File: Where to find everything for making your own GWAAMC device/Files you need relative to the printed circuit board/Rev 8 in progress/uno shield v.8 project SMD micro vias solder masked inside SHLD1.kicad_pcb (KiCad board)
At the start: 2 copper layers, 68.6 x 53.3 mm, 82 parts, among them J1 Conn_3.5mm, J2 Power, J3 Analog, J4 Digital, J5 Digital, J6 Conn_01x09_Female, J6_A7,A6 Conn_01x02_gender_unknown, J7_A7,A6 Conn_01x02_Female, J9 TE_1-2328702-0, P1 CONN_01X01, P2 CONN_01X01, P3 CONN_01X01, P4 CONN_01X01, Q1 MMBF5460 (2N5460), Q2 MMBF5460 (2N5460), Q3 DMN601K-7, Q4 DMN601K-7, Q5 DMN601K-7, Q6 DMN601K-7, Q7 DMN601K-7, U1 3V LDO, U2 AD8244ARMZ, U3 ADL5315ACPZ-R7, U4 REF200AU, U5 LM334M, U6 LM334M, U7 MCP4262-503E/UN, U8 - U32 all in parallel MCP4262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

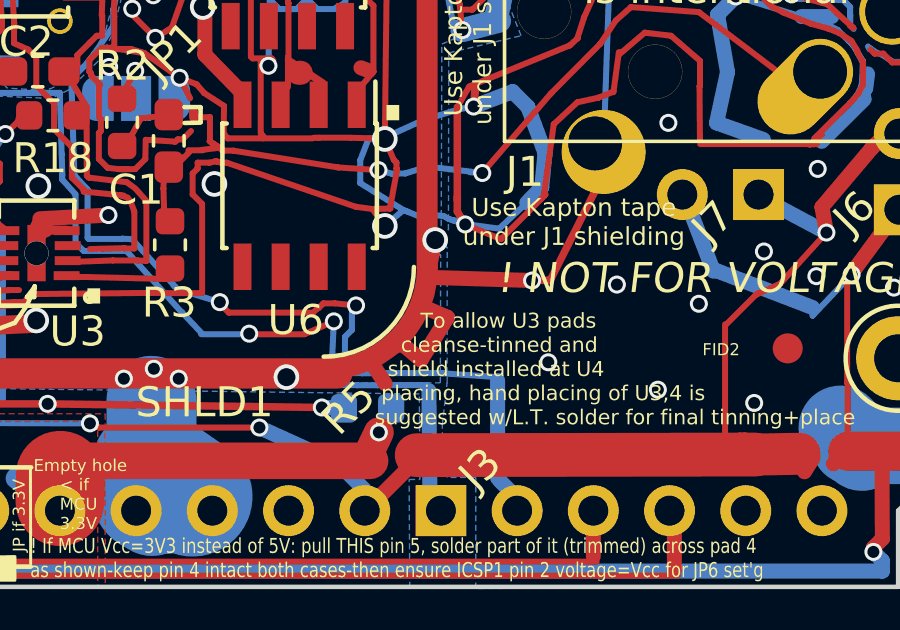
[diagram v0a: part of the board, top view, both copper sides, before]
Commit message: Untested while awaiting bare PCB boards....
These KiCad and zipped gerber files are fully designed but not yet tested while I await the bare boards on order now.  I'm estimating mid- to late-October will see the final evaluation of operation of the entire device.  Shortly after that, I would expect to demonstrate its concepts and operation via YouTube and personal travel.
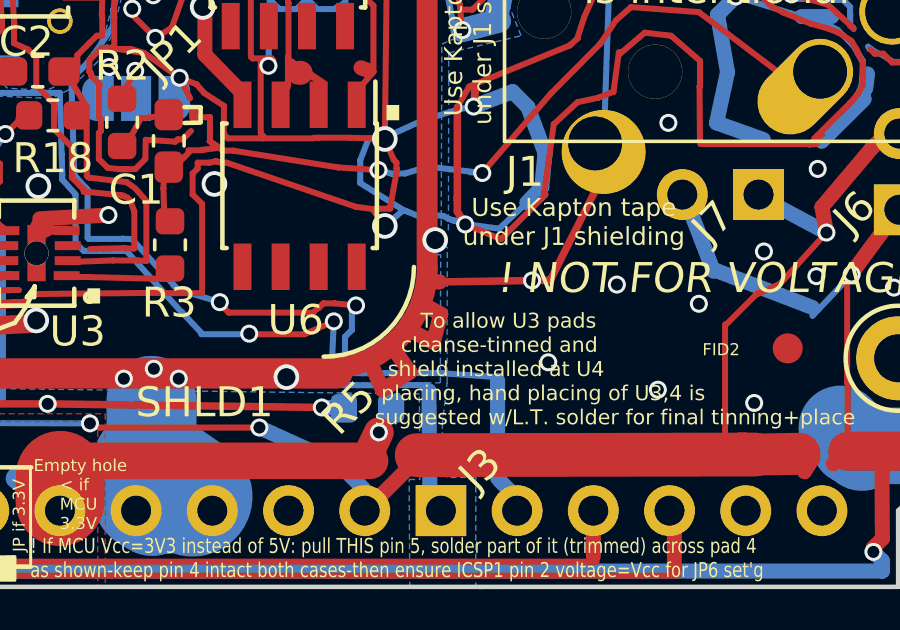
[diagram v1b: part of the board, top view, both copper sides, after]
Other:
- board text added: "10 MASTER"
- board text added: "12 MASTER"
- board text added: "13 MASTER"
- board text added: "2 MASTER"
- board text added: "5 MASTER"
- board text added: "6 MASTER"
- board text added: "8 MASTER"
